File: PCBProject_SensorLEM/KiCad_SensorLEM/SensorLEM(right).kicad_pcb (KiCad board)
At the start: 4 copper layers, 112.7 x 25.5 mm, 79 parts, among them J1 HIF3FC-30PA-2.54DSA, U1 ADR423ARZ

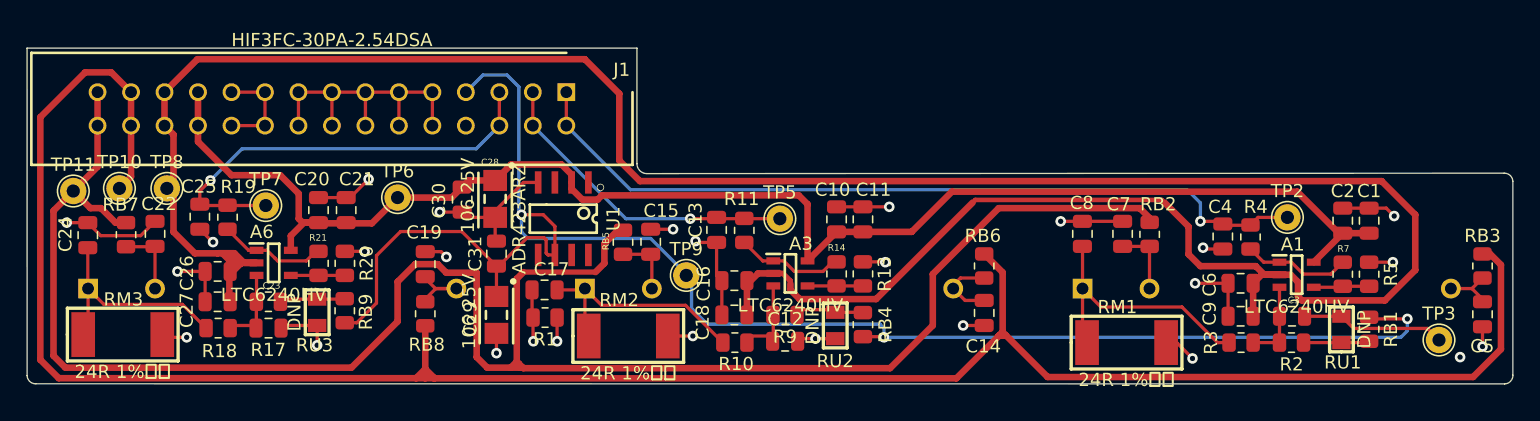
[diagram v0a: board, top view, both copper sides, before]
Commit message: 解决电流传感器中的错误：电线与边缘太近了！
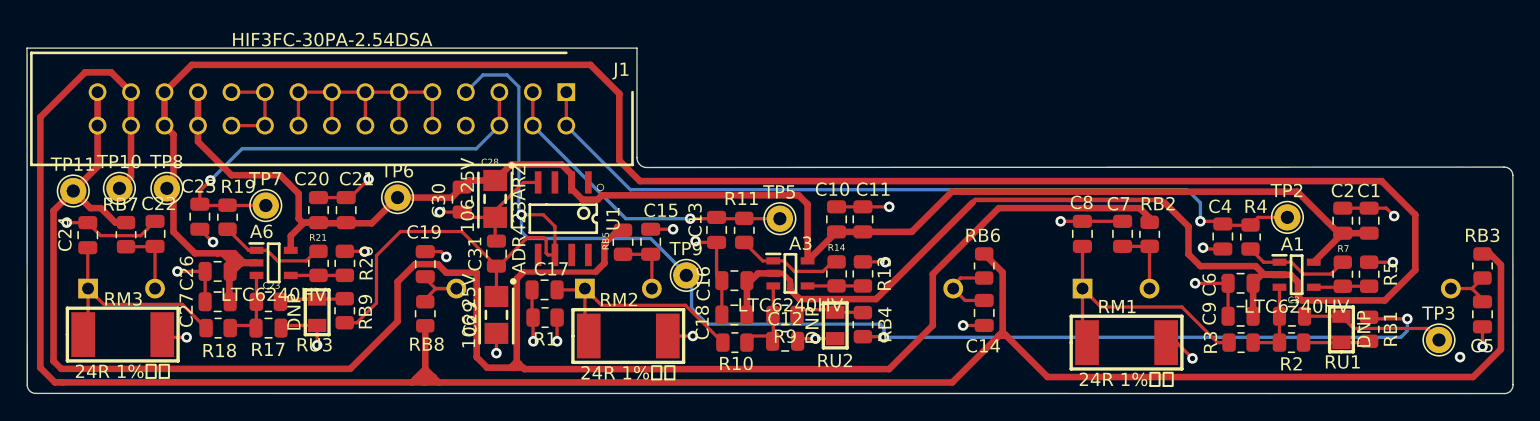
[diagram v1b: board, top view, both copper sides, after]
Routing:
- net +12: track 171.6 -> 174.3 mm
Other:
- board size 112.7 x 25.5 mm -> 112.7 x 26.2 mm
